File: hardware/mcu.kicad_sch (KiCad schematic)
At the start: 26 parts, among them J5 Conn_ARM_JTAG_SWD_10, SW3 SW_Push, U2 EFR32FG28A122F1024GM48-A, U20 USBLC6-2P6, U21 USBLC6-2P6, X1 HF_Crystal, Y1 LF_Crystal

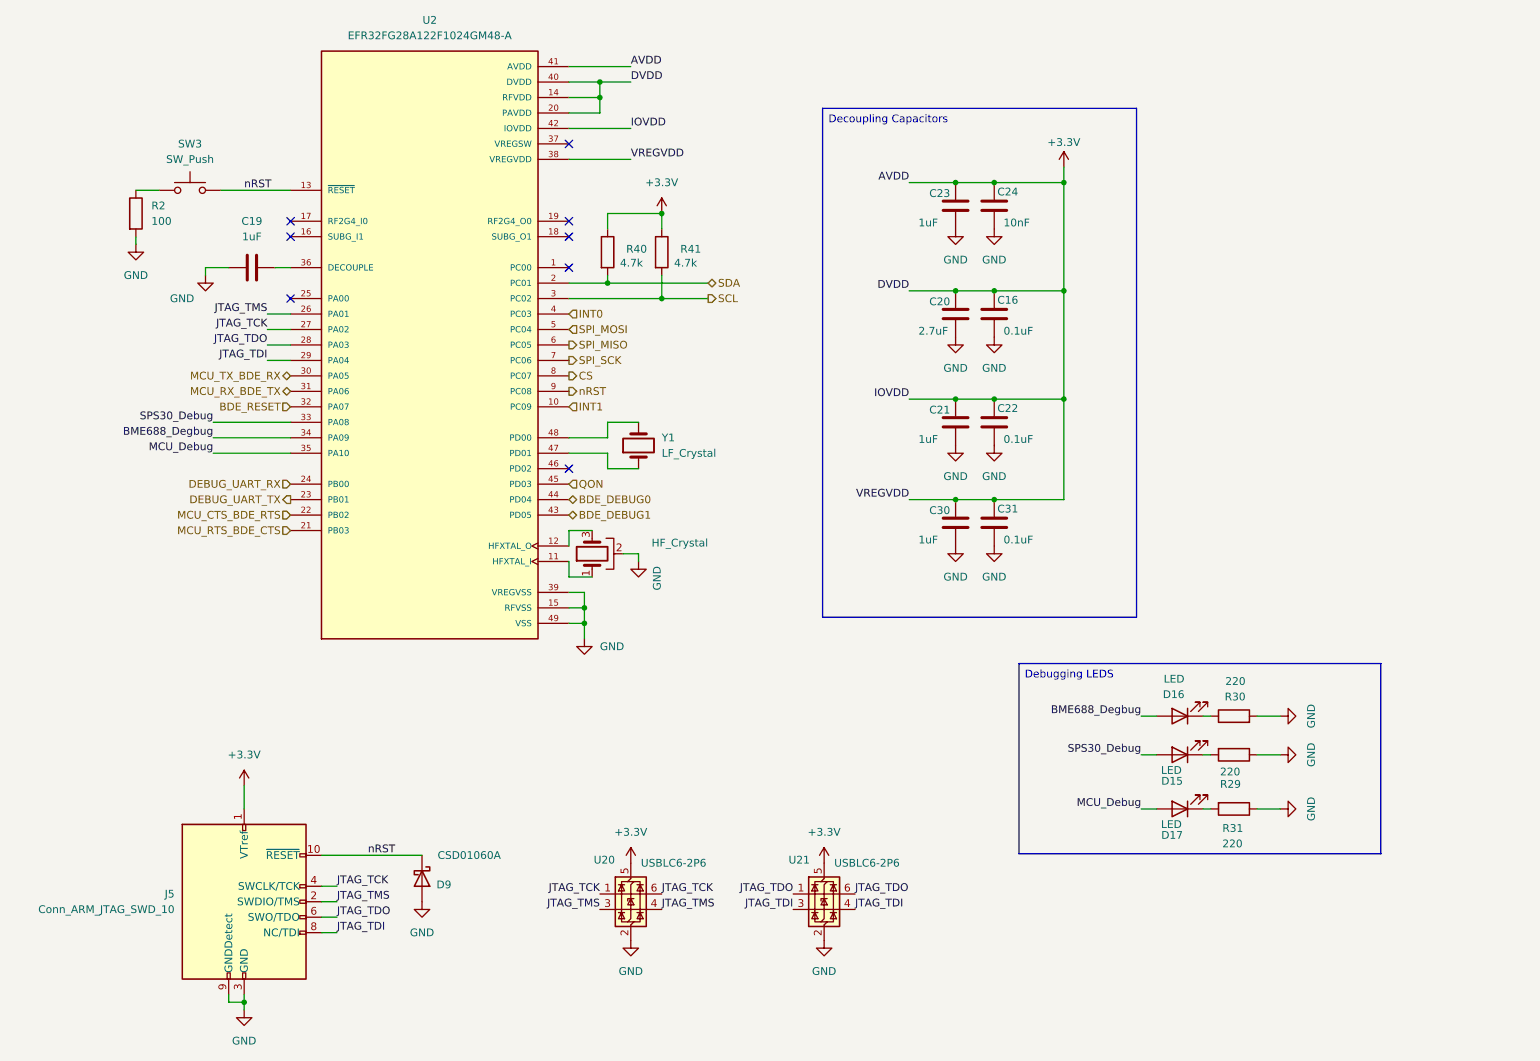
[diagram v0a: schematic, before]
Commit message: updated 5V power and pin
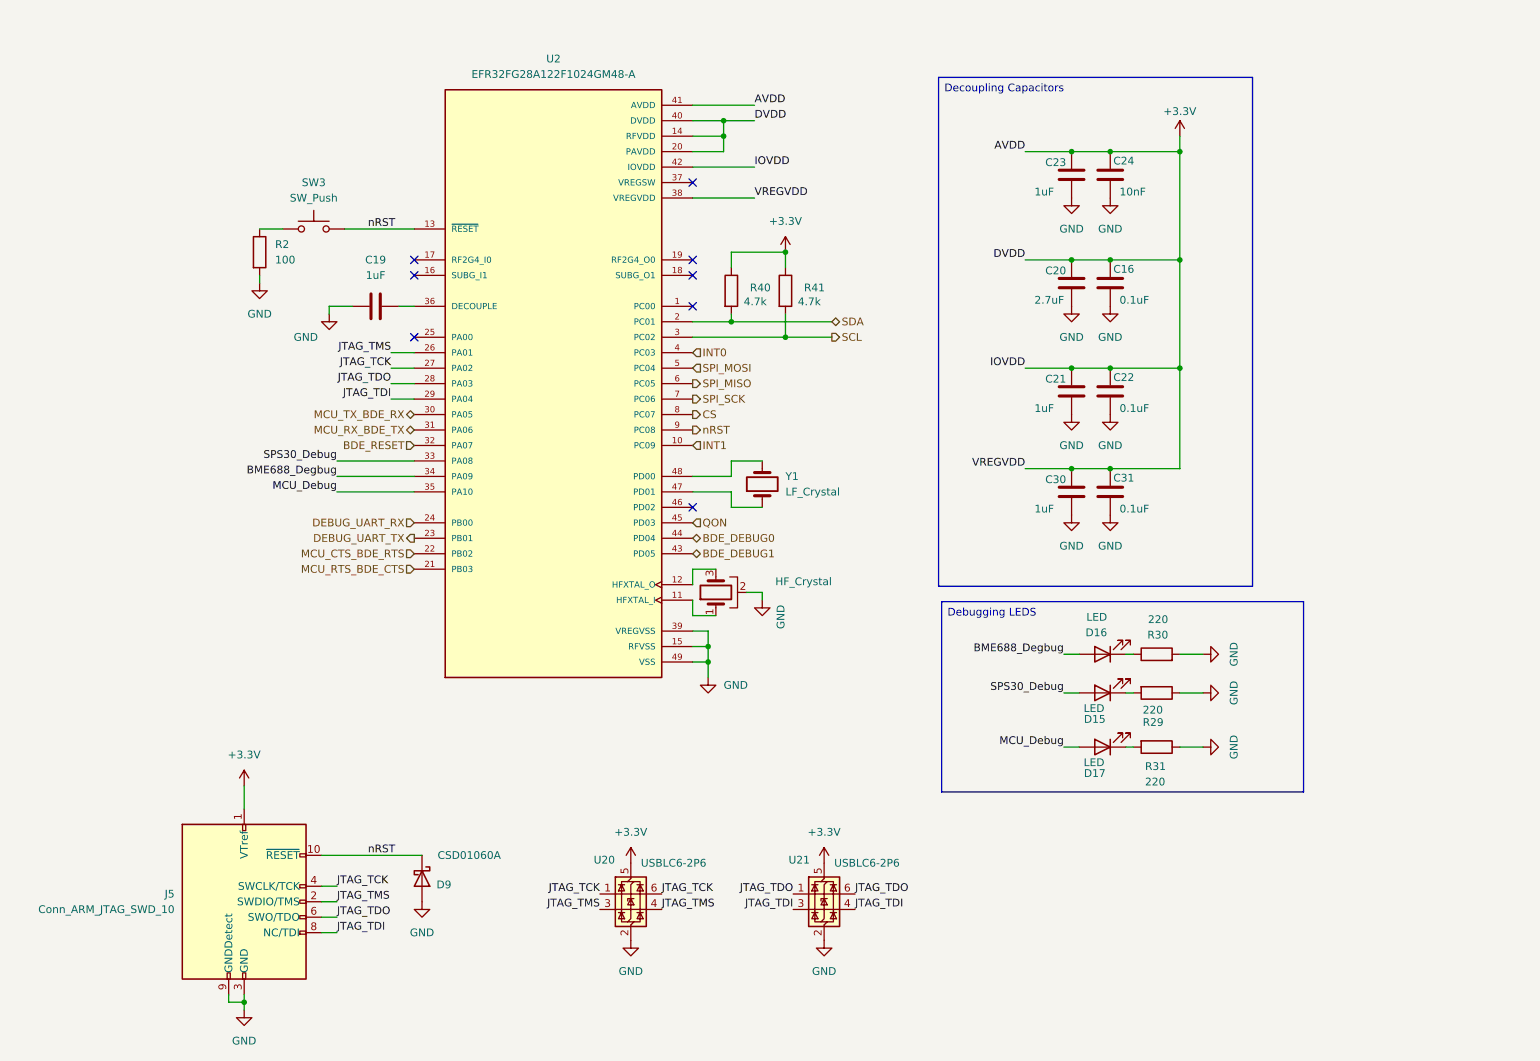
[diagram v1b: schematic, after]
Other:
- moved on the sheet: C16, C19, C20, C21, C22, C23, C24, C30, C31, D15, D16, D17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

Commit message: updated annotations
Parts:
- renumbered C19 to C201, C23 to C202, C20 to C203, C21 to C204, C30 to C205, C24 to C206, C16 to C207, C22 to C208, C31 to C209, D9 to D201, D16 to D202, D15 to D203, D17 to D204, J5 to J201, R2 to R201, R40 to R202, R41 to R203, R30 to R204, R29 to R205, R31 to R206, SW3 to SW201, U2 to U201, U20 to U202, U21 to U203, X1 to X201, Y1 to Y201

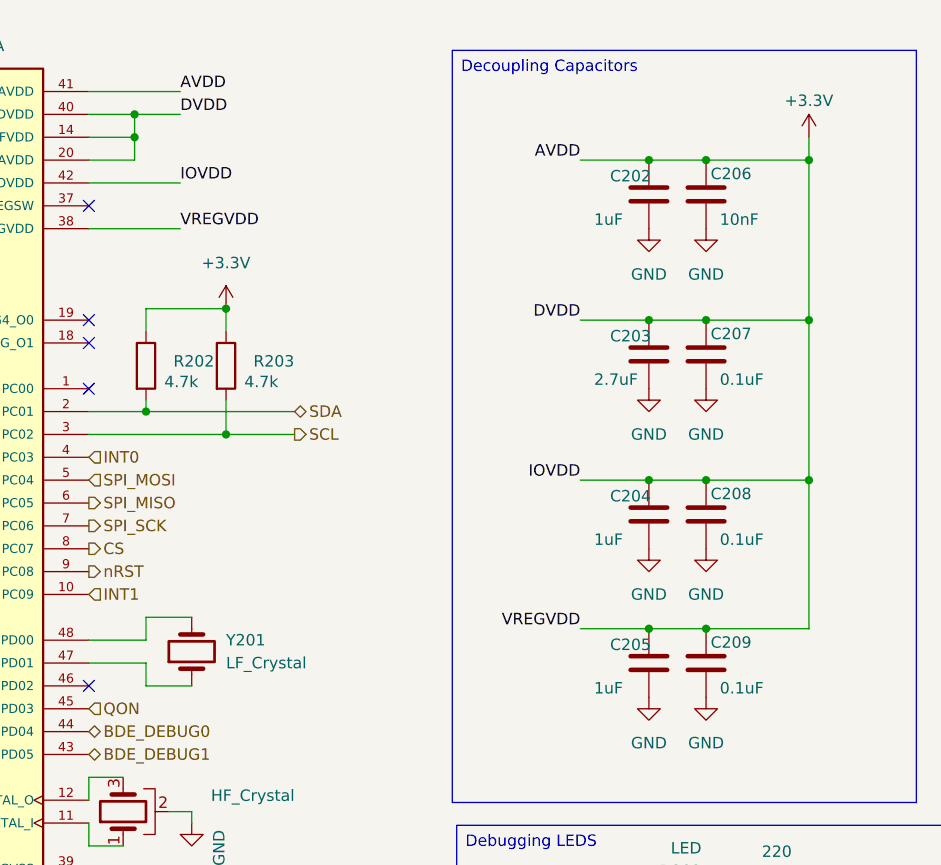
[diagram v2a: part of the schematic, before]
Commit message: added ship fet
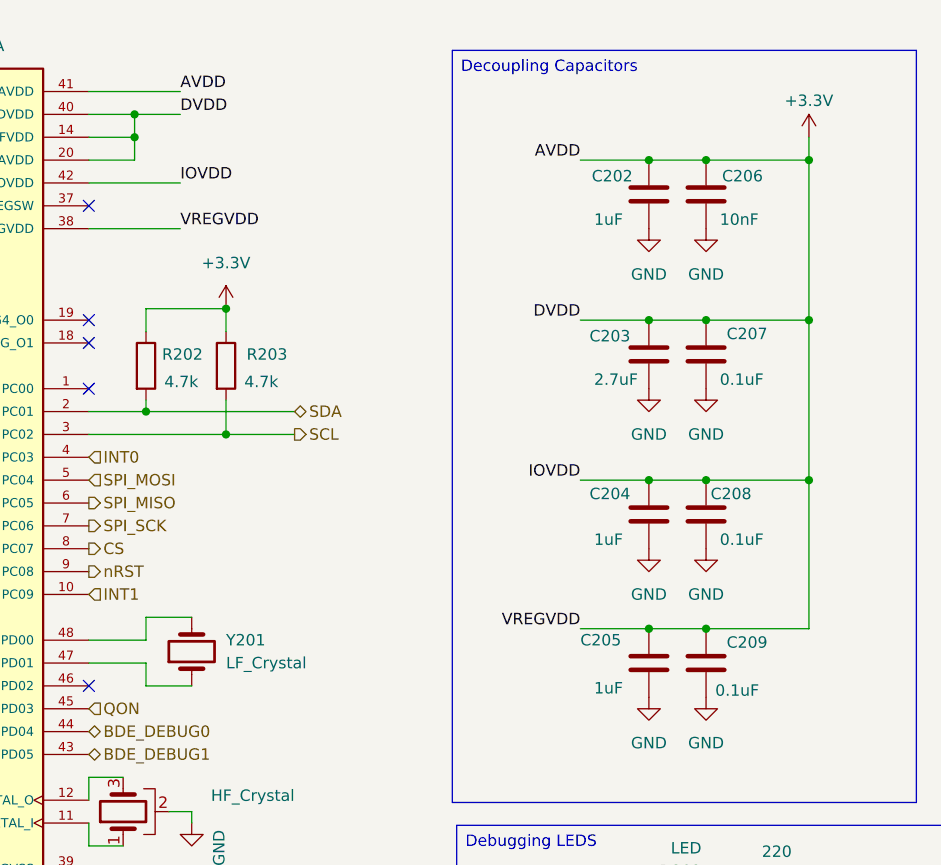
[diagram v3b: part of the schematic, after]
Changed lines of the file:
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@@
 		(dnp no)
 		(property "Reference" "C206"
-			(at 198.628 42.164 0)
+			(at 199.898 42.418 0)
 			(effects
 				(font
@@
 		(dnp no)
 		(property "Reference" "C202"
-			(at 187.452 42.418 0)
+			(at 185.42 42.418 0)
 			(effects
 				(font
@@
 		(dnp no)
 		(property "Reference" "R202"
-			(at 138.938 62.992 0)
+			(at 137.668 62.23 0)
 			(effects
 				(font
@@
 		(dnp no)
 		(property "Reference" "C205"
-			(at 187.452 94.488 0)
+			(at 184.15 93.98 0)
 			(effects
 				(font
@@
 		(dnp no)
 		(property "Reference" "R203"
-			(at 147.828 62.992 0)
+			(at 147.066 62.23 0)
 			(effects
 				(font
@@
 		(dnp no)
 		(property "Reference" "C204"
-			(at 187.452 77.978 0)
+			(at 185.166 77.724 0)
 			(effects
 				(font
@@
 		(dnp no)
 		(property "Reference" "C209"
-			(at 198.628 94.234 0)
+			(at 200.406 94.234 0)
 			(effects
 				(font
@@
 		)
 		(property "Value" "0.1uF"
-			(at 199.644 99.314 0)
+			(at 199.136 99.568 0)
 			(effects
 				(font
@@
 		(dnp no)
 		(property "Reference" "C203"
-			(at 187.452 60.198 0)
+			(at 185.166 60.198 0)
 			(effects
 				(font
@@
 		(dnp no)
 		(property "Reference" "C207"
-			(at 198.628 59.944 0)
-			(effects
-				(font
+			(at 200.406 59.944 0)
+			(effects
+				(font

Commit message: footprint update
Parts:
- C201: footprint Capacitor_SMD:C_0402_1005Metric -> Capacitor_SMD:C_0805_2012Metric
- C202, C203, C204, C205, C206, C207, C208, C209: footprint (none) -> Capacitor_SMD:C_0805_2012Metric
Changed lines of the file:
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@@
 			)
 		)
-		(property "Footprint" "Capacitor_SMD:C_0402_1005Metric"
+		(property "Footprint" "Capacitor_SMD:C_0805_2012Metric"
 			(at 81.28 65.0748 0)
 			(effects
@@
 			)
 		)
-		(property "Footprint" ""
+		(property "Footprint" "Capacitor_SMD:C_0805_2012Metric"
 			(at 199.0852 48.26 0)
 			(effects
@@
 			)
 		)
-		(property "Footprint" ""
+		(property "Footprint" "Capacitor_SMD:C_0805_2012Metric"
 			(at 199.0852 83.82 0)
 			(effects
@@
 			)
 		)
-		(property "Footprint" ""
+		(property "Footprint" "Capacitor_SMD:C_0805_2012Metric"
 			(at 192.7352 48.26 0)
 			(effects
@@
 			)
 		)
-		(property "Footprint" ""
+		(property "Footprint" "Capacitor_SMD:C_0805_2012Metric"
 			(at 192.7352 100.33 0)
 			(effects
@@
 			)
 		)
-		(property "Footprint" ""
+		(property "Footprint" "Capacitor_SMD:C_0805_2012Metric"
 			(at 192.7352 83.82 0)
 			(effects
@@
 			)
 		)
-		(property "Footprint" ""
+		(property "Footprint" "Capacitor_SMD:C_0805_2012Metric"
 			(at 199.0852 100.33 0)
 			(effects
@@
 			)
 		)
-		(property "Footprint" ""
+		(property "Footprint" "Capacitor_SMD:C_0805_2012Metric"
 			(at 192.7352 66.04 0)
 			(effects
@@
 			)
 		)
-		(property "Footprint" ""
+		(property "Footprint" "Capacitor_SMD:C_0805_2012Metric"
 			(at 199.0852 66.04 0)
 			(effects

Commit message: footprint update 2
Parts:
- D201: footprint Package_TO_SOT_THT:TO-220-2_Vertical -> Diode_SMD:D_SOD-123
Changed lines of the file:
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@@
 			)
 		)
-		(property "Footprint" "Package_TO_SOT_THT:TO-220-2_Vertical"
+		(property "Footprint" "Diode_SMD:D_SOD-123"
 			(at 80.645 160.02 0)
 			(effects

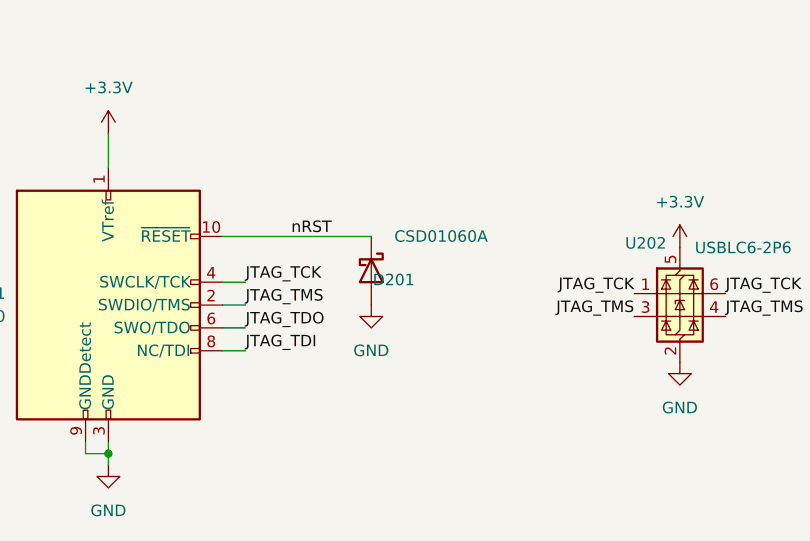
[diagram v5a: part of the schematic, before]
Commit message: updated ESD/Inductor footprints
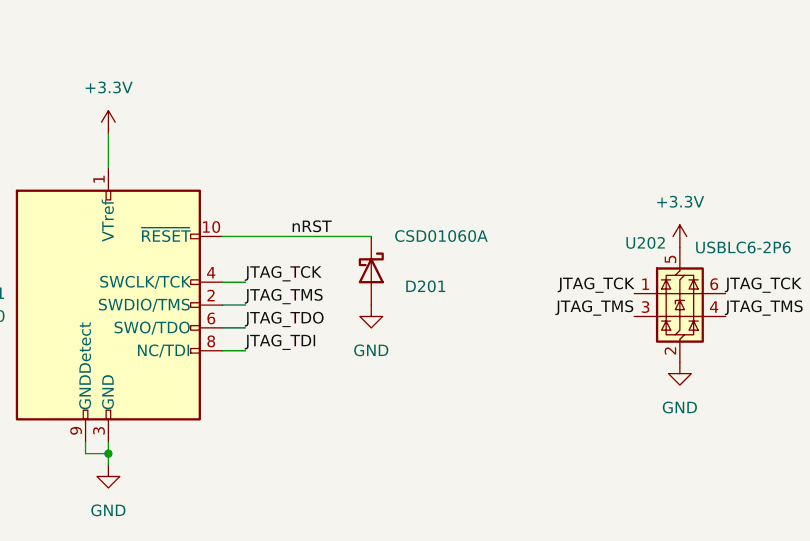
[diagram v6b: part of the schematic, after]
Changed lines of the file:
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@@
 		(dnp no)
 		(property "Reference" "D201"
-			(at 89.916 161.036 90)
+			(at 93.472 161.798 90)
 			(effects
 				(font

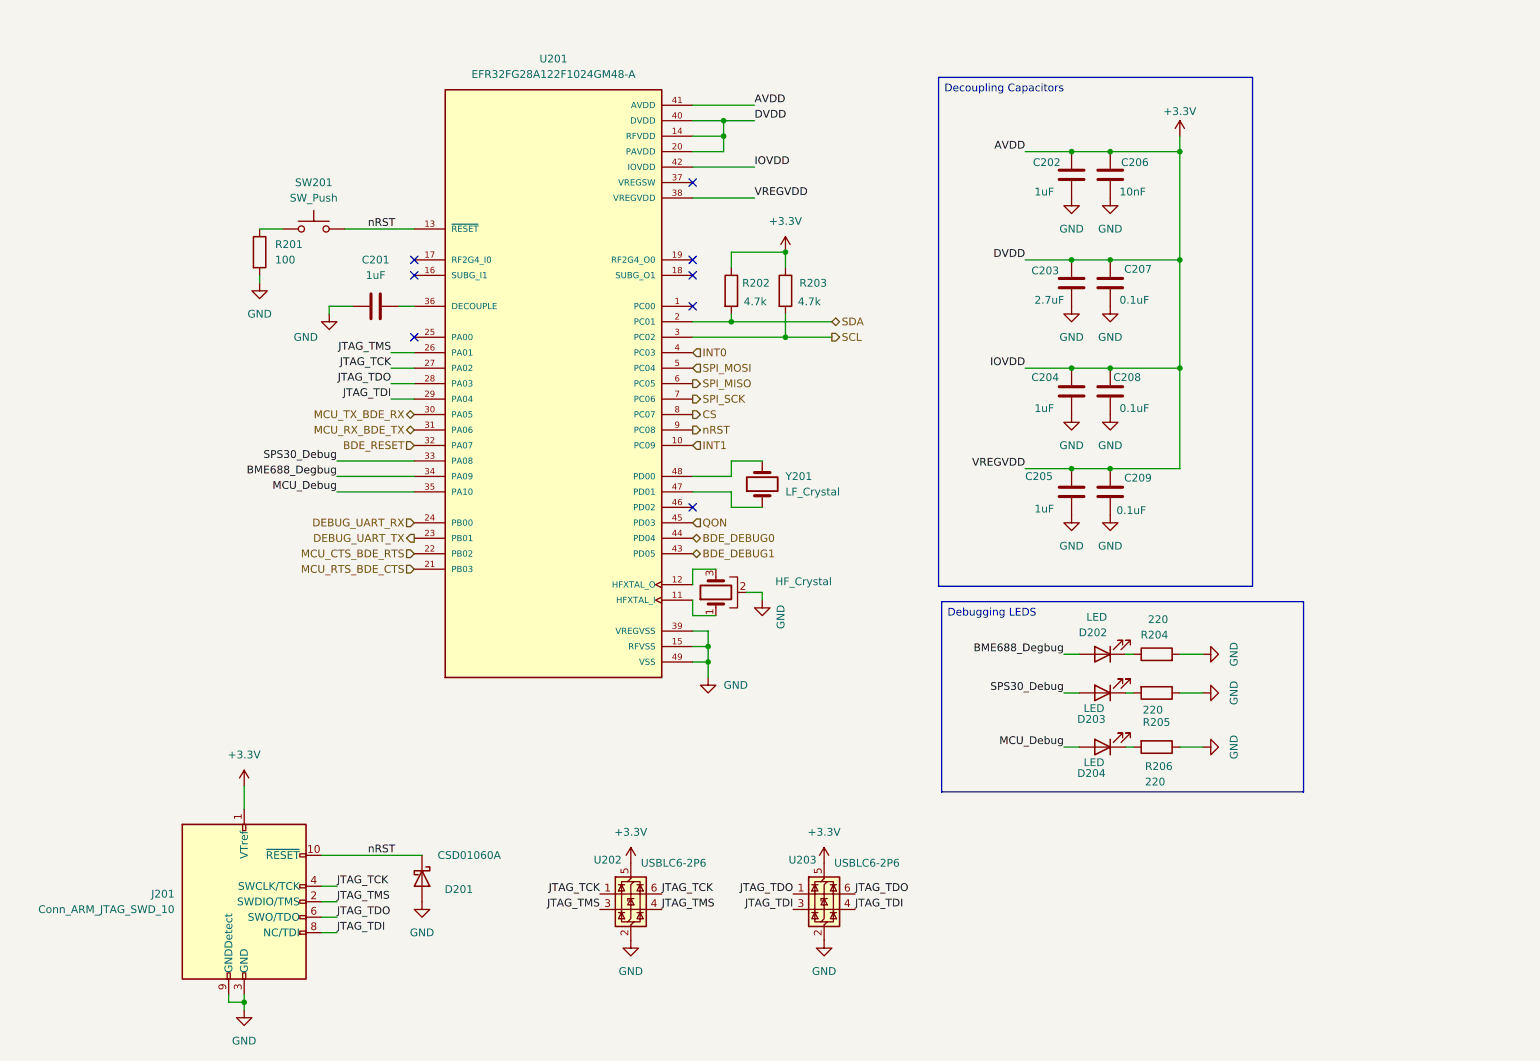
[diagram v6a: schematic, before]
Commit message: updated footprints
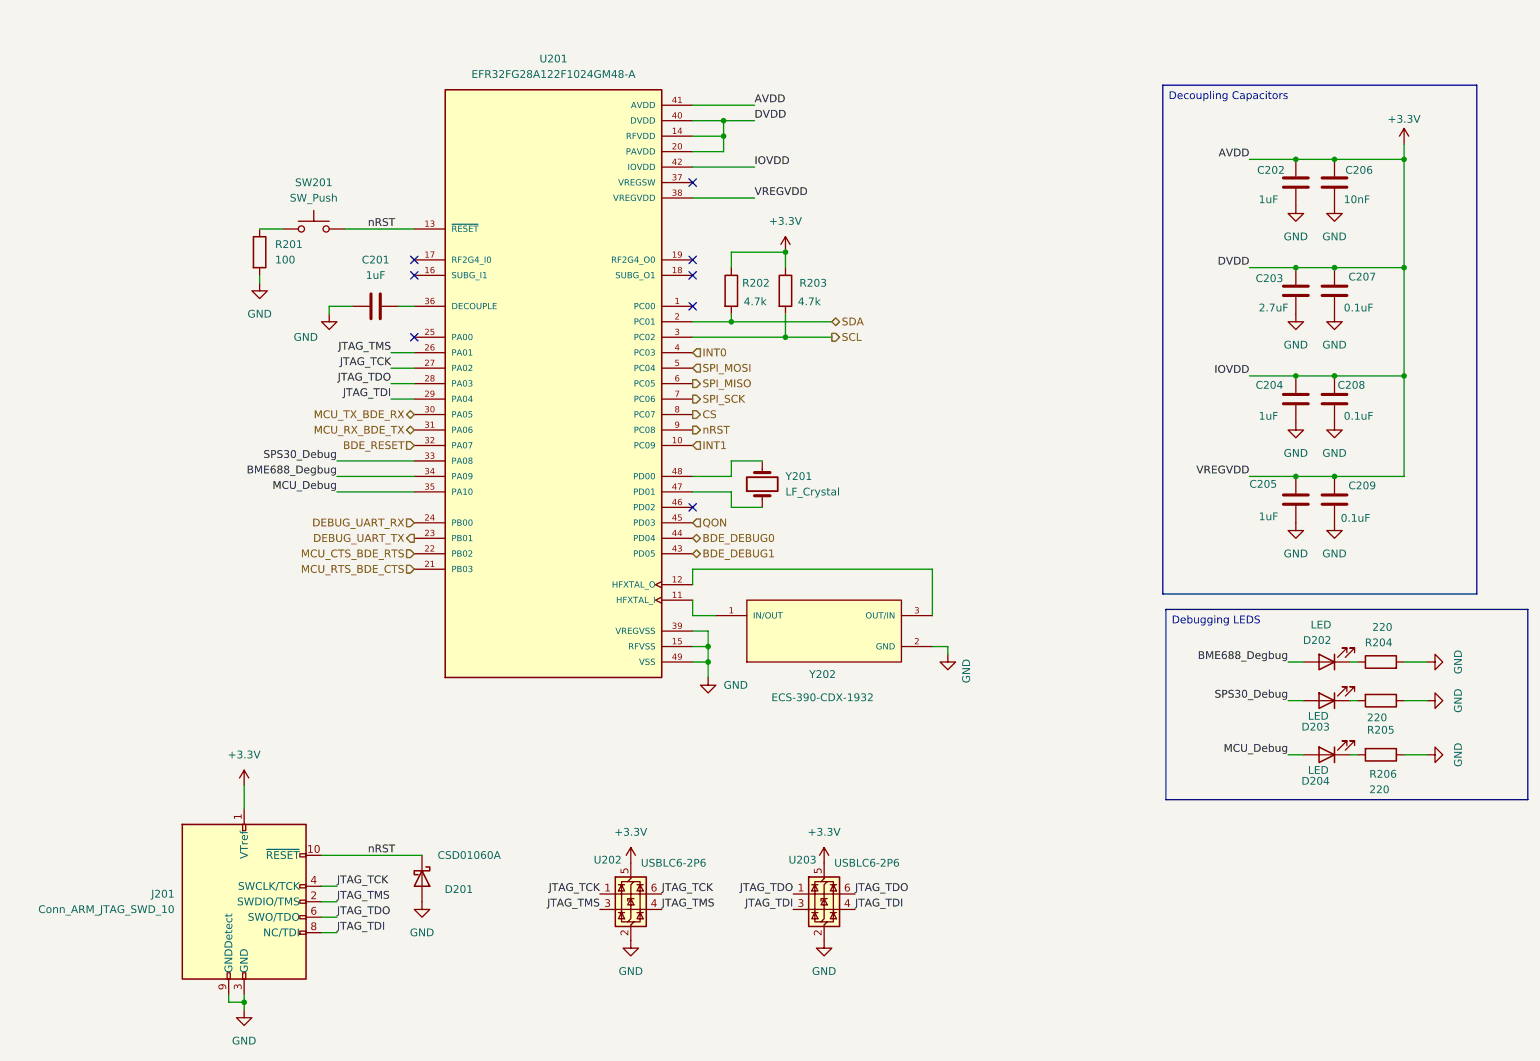
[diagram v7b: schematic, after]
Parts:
- removed X201: HF_Crystal, Crystal:Crystal_SMD_2016-4Pin_2.0x1.6mm, symbol Device:Crystal_GND2
- added Y202: ECS-390-CDX-1932, pyronet_footprints:XTAL_ECS-390-CDX-1932, symbol pyronet_symbols:ECS-390-CDX-1932
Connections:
- net GND: now also Y202.2 (GND), Y202.4 (GND__1)
- net at U201.11 (HFXTAL_I): now also Y202.1 (IN/OUT)
- net at U201.12 (HFXTAL_O): now also Y202.3 (OUT/IN)
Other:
- moved on the sheet: C202, C203, C204, C205, C206, C207, C208, C209, D202, D203, D204, R204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
